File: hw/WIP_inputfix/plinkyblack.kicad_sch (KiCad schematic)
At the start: 265 parts, among them J1 AudioJack2_SwitchT, J10 AudioJack2_SwitchT, J11 AudioJack2_SwitchT, J12 Conn_02x08_Odd_Even, J13 Conn_02x08_Odd_Even, J14 AudioJack2_SwitchT, J15 AudioJack2_SwitchT, J16 AudioJack2_SwitchT, J17 AudioJack2_SwitchT, J18 USB_B_Micro, J19 SJ1-3523N, J2 AudioJack2_SwitchT, J20 oled0.91, J21 SJ1-3523N, J22 AudioJack2_SwitchT, J23 AudioJack2_SwitchT, J24 USB_B_Micro, J25 Conn_01x16_Female, J26 SJ1-3523N, J27 SJ1-3523N, J3 AudioJack2_SwitchT, J4 AudioJack2_SwitchT, J5 SWD header, J6 AudioJack2_SwitchT, J7 AudioJack2_SwitchT, J8 AudioJack2_SwitchT, J9 AudioJack2_SwitchT, Q1 MMBT3904, U1 MCP6002-xSN, U10 TL072, U11 TL072, U12 W25Q32JVSS, U13 TPS61040DBV, U14 W25Q32JVSS, U15 USBLC6-2SC6, U16 TL072, U17 LIS2DH12, U18 TL072, U2 LM1117-3.3, U3 LM1117-3.3, U4 STM32L476VGTx, U5 TL072, U6 WM8758B, U7 TL072, U8 MCP6002-xSN, U9 MCP6002-xSN, Y1 Crystal_GND24

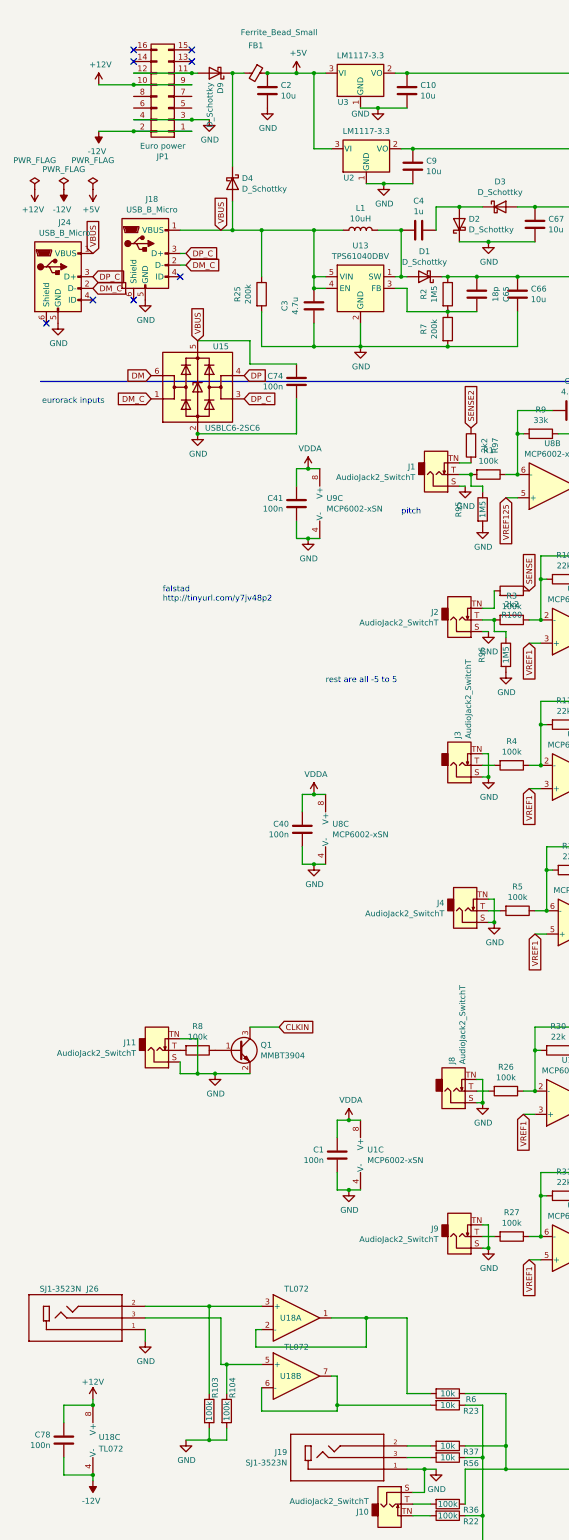
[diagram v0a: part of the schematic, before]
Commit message: Initial Clean Up Run
- change many passives to 0402
- change TL072's to the same SOIC package
- finish up routing for topside input buffer
- add diodes for +- 12 from eurorack input (untested)
- change some board limits to represent current manufacturing reality
- hunt down a lot of DRC errors (lots of warnings remaining!)
- made hole for expander bigger
- fixedsys fonts + text label moving about
- todo: reset labels for 0402 parts since my standard library has the labels taken off.
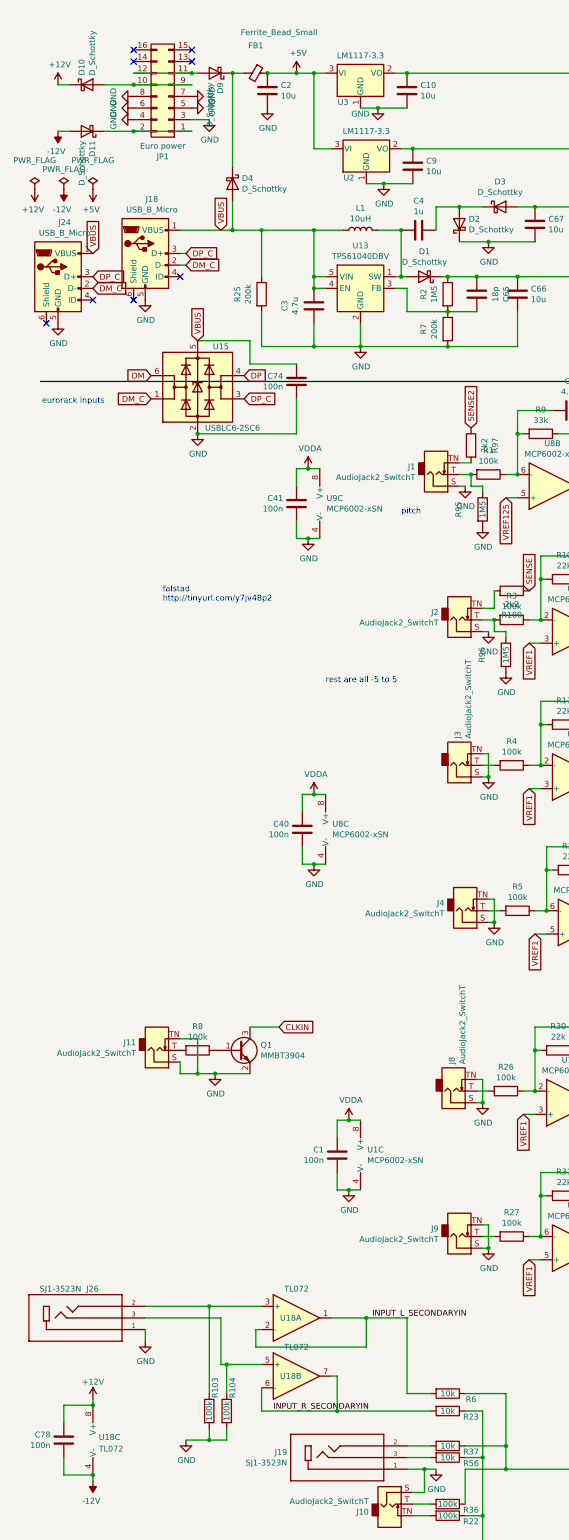
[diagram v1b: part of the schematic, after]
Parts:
- added D10, D11: D_Schottky, Diode_SMD:D_SMA, symbol Device:D_Schottky
- C1, C11, C16, C17, C18, C19, C22, C23, C25, C28, C34, C35, C36, C37, C4, C40, C41, C50, C51, C52, C53, C54, C56, C57, C58, C59, C64, C68, C69, C70, C73, C74, C77, C78: footprint Capacitor_SMD:C_0603_1608Metric -> Capacitor_SMD:C_0402_1005Metric
- R1, R10, R101, R102, R103, R104, R106, R11, R12, R13, R14, R15, R18, R19, R22, R23, R26, R27, R28, R3, R30, R31, R32, R33, R34, R36, R37, R4, R42, R43, R44, R45, R46, R47, R48, R49, R5, R50, R51, R56, R6, R66, R67, R8, R83, R84, R85, R86, R87, R88, R89, R9, R90, R98, R99: footprint Resistor_SMD:R_0603_1608Metric -> Resistor_SMD:R_0402_1005Metric
- U18: footprint Package_TO_SOT_SMD:SOT-23-8 -> Package_SO:SOIC-8_3.9x4.9mm_P1.27mm
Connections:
- net +12V: now also D10.1 (K); no longer JP1.10 (Pin_10), JP1.9 (Pin_9)
- net -12V: now also D11.2 (A); no longer JP1.1 (Pin_1), JP1.2 (Pin_2)
- net GND: now also JP1.5 (Pin_5), JP1.6 (Pin_6), JP1.7 (Pin_7), JP1.8 (Pin_8)
- net INPUT_L_SECONDARYIN: now reaches R6.2, U18.1, U18.2 (-)
- net INPUT_R_SECONDARYIN: now reaches R23.2, U18.6 (-), U18.7
- new net: D11.1 (K), JP1.1 (Pin_1), JP1.2 (Pin_2)
- new net: D10.2 (A), JP1.10 (Pin_10), JP1.9 (Pin_9)
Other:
- moved on the sheet: R23
